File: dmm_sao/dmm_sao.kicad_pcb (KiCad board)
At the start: 2 copper layers, 34 x 68 mm, 63 parts, among them J1 RED_MEASURE, J2 BLK_GND, J3 USB_C, Q1 CJ2302, Q2 CJ2305, SW1 TS5220A, SW2 RotaryEncoder, SW3 TS5220A, SW4 TS5220A, U1 HX9193-33GB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

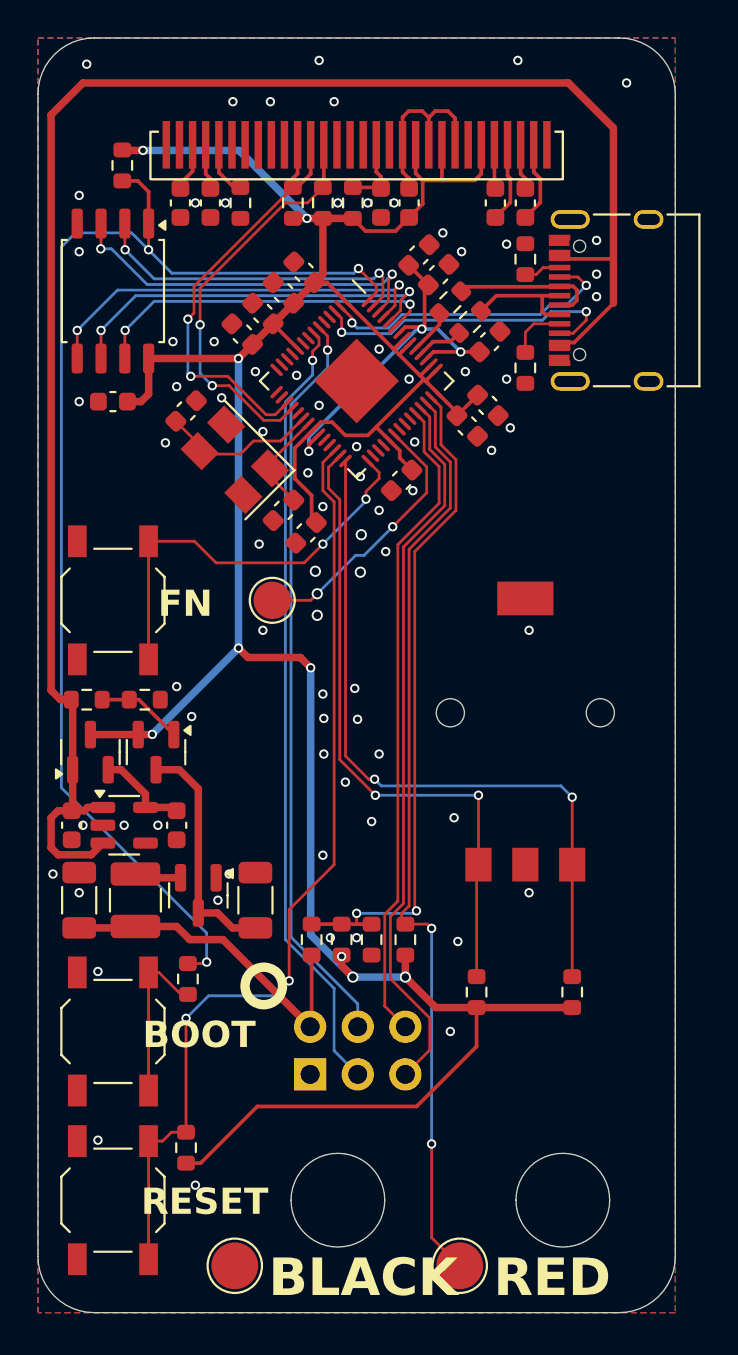
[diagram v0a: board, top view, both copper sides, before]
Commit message: Moved buzzer to base board
Also:
- Moved a few parts to make space for the buzzer
- Connected the buzzer in a push/pull setup for better volume
- Changed the edgecut a little, to have better space for knob intent mechanism in case
- Tweaked pads for spring loaded pins to match manufacturer suggestion
- Made the paste for the display connector 10% smaller

Signed-off-by: Thomas Flummer <tf@flummer.net>
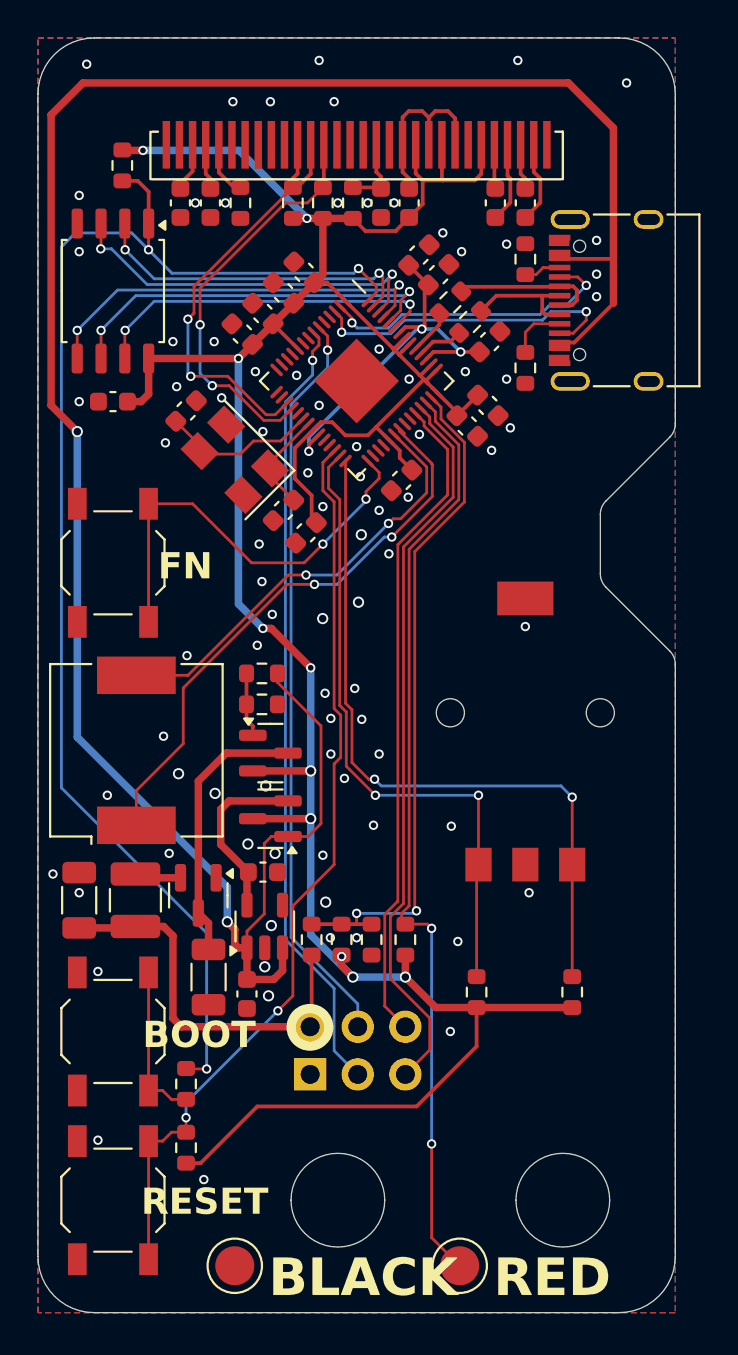
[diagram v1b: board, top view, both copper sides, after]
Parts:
- removed TP1: Buzzer, TestPoint:TestPoint_Pad_D2.0mm
- added LS1: OWPB-909018S-40-03, Buzzer_Beeper:Buzzer_CUI_CPT-9019S-SMT, F.Cu at (88.2, 104.0)
- added SCREEN_SUPPORT: Case, Aesthetics:Case, F.Cu at (83.0, 66.0)
- moved C7 13.0 mm to (94.2, 117.0)
- moved Q1 10.2 mm to (95.4, 107.7), turned to 180 degrees
- moved R9 9.45 mm to (95.0, 99.9), turned to 180 degrees
- moved U1 9.24 mm to (95.1, 113.4), turned to 90 degrees
- moved R10 6.25 mm to (95.0, 101.5)
- moved Q2 6.10 mm to (95.4, 104.2), turned to 0 degrees
- moved R13 5.60 mm to (90.9, 121.8)
- moved C9 5.24 mm to (95.0, 110.5), turned to 0 degrees
- moved C10 4.80 mm to (92.1, 116.1), turned to -90 degrees
- moved SW1 2.00 mm to (87.0, 94.0)
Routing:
- net /RP2040/SPI_COPI/G7: track 0.00 -> 30.2 mm, vias 0 -> 2
- net USB_BUS_POWER: track 93.4 -> 120.1 mm, vias 0 -> 2
- net /RP2040/SPI_SCK/G6: track 14.4 -> 23.3 mm
- net /RP2040/QSPI-~{CS}: track 66.6 -> 72.4 mm
- net VCC: track 162.6 -> 157.6 mm, vias 9 -> 10
- net /PSU/VREG_OUT: track 4.97 -> 9.42 mm
- net SAO_VIN: track 18.4 -> 21.0 mm
- net /PSU/BOOST_OUT: track 12.7 -> 14.6 mm
- net /RP2040/~{RESET}: track 50.7 -> 48.9 mm
- net Net-(Q2-G): track 4.60 -> 3.44 mm
- net BTN_FN: track 22.4 -> 23.2 mm
- net GND: vias 78 -> 85
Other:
- outline, holes or cut-outs redrawn
- board text added: "1.1, matching SAO v. 1.69bis"
- board text removed: "1.0, matching SAO v. 1.69bis"

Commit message: Added logos and adjusted panel tooling holes
Tool holes changed to be 1.152mm diameter, following JLCPCB assembly spec

versions bumped to 1.2

Signed-off-by: Thomas Flummer <tf@flummer.net>
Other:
- board text added: "1.2, matching SAO v. 1.69bis"
- board text removed: "1.1, matching SAO v. 1.69bis"
